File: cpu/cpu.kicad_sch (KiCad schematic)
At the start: 44 parts, among them J2 Conn_01x08, Q1 AO3401A, Q2 RU1J002YN, Q3 RU1J002YN, U1 ICE40HX1K-VQ100_RV4028, U2 W25Q80DVSS, U3 AP2112K-1.2

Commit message: Improve power.  Start work on IO module
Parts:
- removed Q1: AO3401A, Package_TO_SOT_SMD:SOT-23, symbol Transistor_FET:AO3401A
- removed Q2: RU1J002YN, Package_TO_SOT_SMD:SOT-323_SC-70, symbol Transistor_FET:2N7002
- removed R8: 39k, Resistor_SMD:R_0603_1608Metric, symbol Device:R
- removed R9: 3k3, Resistor_SMD:R_0603_1608Metric, symbol Device:R
- removed TP2: Test, TestPoint:TestPoint_Pad_1.5x1.5mm, symbol Connector:TestPoint
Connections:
- net VCCIO is gone; now on net +3V3: C11.2, C12.2, C13.2, C14.2, C15.2, C16.2, C17.2, C18.2, C19.2, C5.1, D1.2 (A), R10.1, R11.1, R3.1, R4.1, R5.1, R6.1, U1.14 (VCCIO_3), U1.22 (VCCIO_3), U1.31 (VCCIO_2), U1.38 (VCCIO_2), U1.50 (VCC_SPI), U1.58 (VCCIO_1), U1.6 (VCCIO_3), U1.67 (VCCIO_1), U1.72 (NC), U1.88 (VCCIO_0), U1.92 (VCCIO_0)
- net +3V3: no longer C3.1, U3.1 (VIN), U3.3 (EN)
- net +5V: now reaches J1.78 (+5V)
- net +5V: now also C3.1, U3.1 (VIN), U3.3 (EN)
- no-connect marks 10 -> 9
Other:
- moved on the sheet: C3, C4, C6, U3

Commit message: RAM module, many tweaks
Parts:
- Q3: value RU1J002YN -> 2N7002; footprint Package_TO_SOT_SMD:SOT-323_SC-70 -> Package_TO_SOT_SMD:SOT-23; JLC C2842817 -> C8545
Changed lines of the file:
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@@
 			)
 		)
-		(property "Value" "RU1J002YN"
+		(property "Value" "2N7002"
 			(at 255.27 120.6499 0)
 			(effects
@@
 			)
 		)
-		(property "Footprint" "Package_TO_SOT_SMD:SOT-323_SC-70"
+		(property "Footprint" "Package_TO_SOT_SMD:SOT-23"
 			(at 254 121.285 0)
 			(effects
@@
 			)
 		)
-		(property "JLC" "C2842817"
+		(property "JLC" "C8545"
 			(at 248.92 119.38 0)
 			(effects

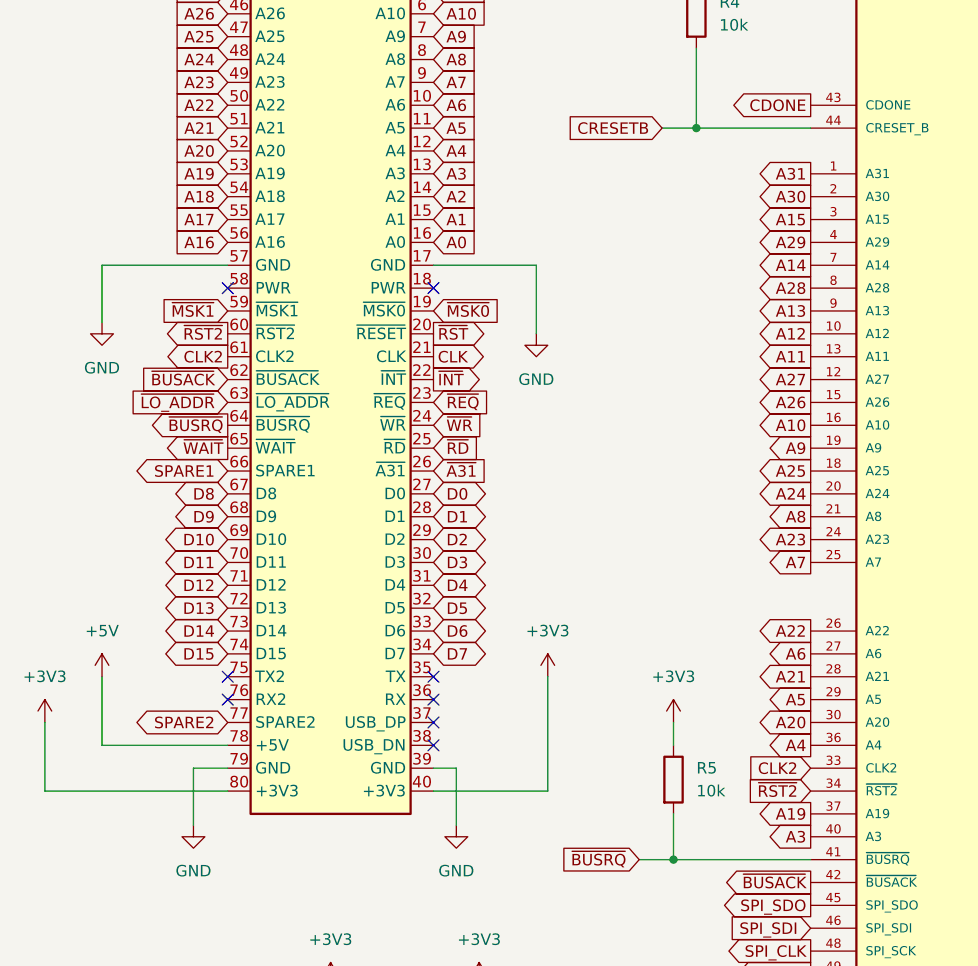
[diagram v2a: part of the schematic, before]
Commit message: Revised module header
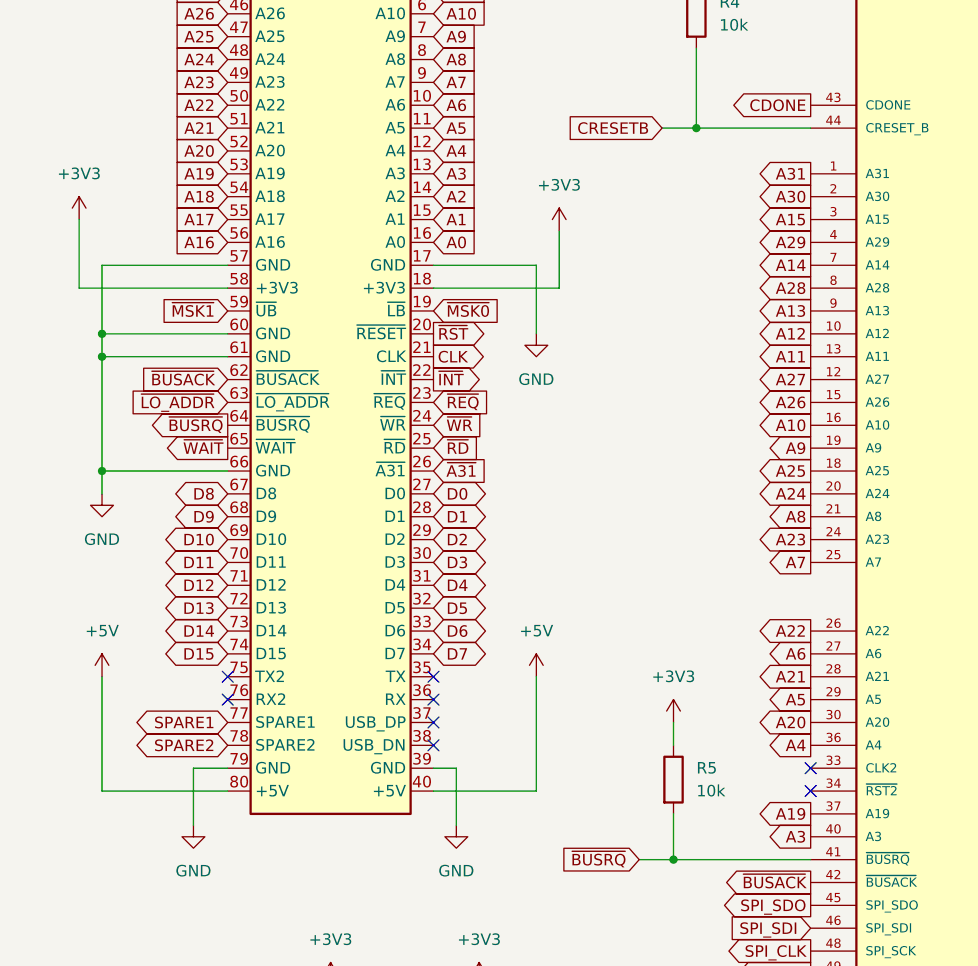
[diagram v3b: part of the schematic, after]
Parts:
- J1: footprint RV4028:ModuleHeader -> RV4028:Module_2mm
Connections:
- net +3V3: now also J1.18 (+3V3), J1.58 (+3V3); no longer J1.40 (+3V3), J1.80 (+3V3)
- net +5V: now also J1.40 (+5V), J1.80 (+5V); no longer J1.78 (+5V)
- net GND: now also J1.60 (GND), J1.61 (GND), J1.66 (GND)
- net SPARE1: now also J1.77 (SPARE1); no longer J1.66 (SPARE1)
- net SPARE2: now also J1.78 (SPARE2); no longer J1.77 (SPARE2)
- net CLK2: no longer names the net of U1.33 (CLK2)
- net CLK2: no longer J1.61 (CLK2)
- net ~{RST2}: no longer names the net of U1.34 (~{RST2})
- net ~{RST2}: no longer J1.60 (~{RST2})

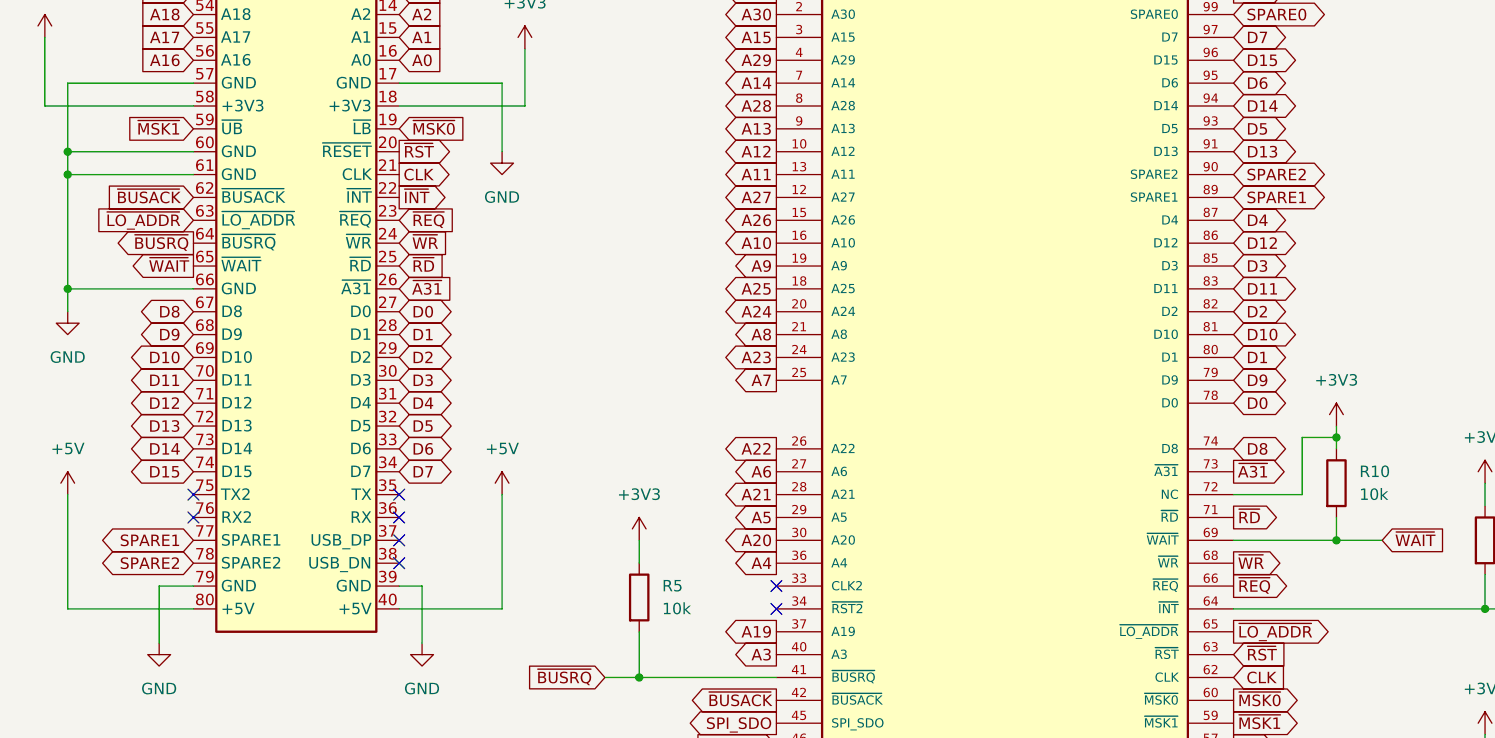
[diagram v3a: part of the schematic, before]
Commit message: IO module 2mm headers
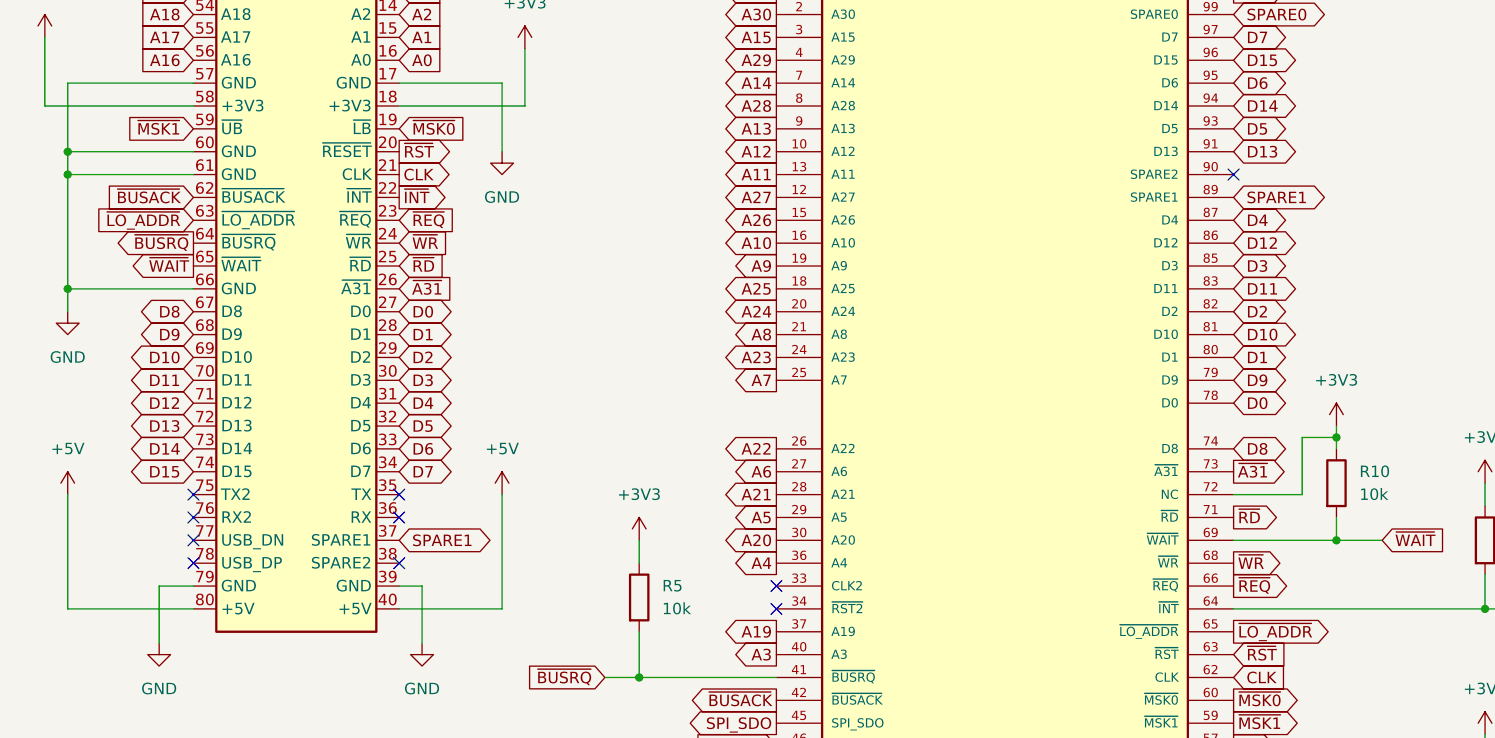
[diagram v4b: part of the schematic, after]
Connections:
- net SPARE1: now also J1.37 (SPARE1); no longer J1.77 (SPARE1)
- net SPARE2: no longer names the net of J1.78 (USB_DP)
- net SPARE2: no longer U1.90 (SPARE2)
- no-connect marks 9 -> 11
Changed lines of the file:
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@@
 	)
 	(no_connect
+		(at 152.4 78.74)
+	)
+	(no_connect
 		(at 152.4 40.64)
 	)
 	(no_connect
+		(at 36.83 121.92)
+	)
+	(no_connect
 		(at 36.83 114.3)
 	)
 	(no_connect
-		(at 59.69 119.38)
+		(at 36.83 119.38)
 	)
 	(wire
@@
 		)
 	)
+	(global_label "SPARE1"
+		(shape bidirectional)
+		(at 59.69 119.38 0)
+		(fields_autoplaced yes)
+		(effects
+			(font
+				(size 1.27 1.27)
+			)
+			(justify left)
+		)
+		(property "Intersheetrefs" "${INTERSHEET_REFS}"
+			(at 70.9831 119.38 0)
+			(effects
+				(font
+					(size 1.27 1.27)
+				)
+				(justify left)
+				(hide yes)
+			)
+		)
+	)
 	(global_label "D10"
 		(shape bidirectional)
@@
 		)
 	)
-	(global_label "SPARE1"
-		(shape bidirectional)
-		(at 36.83 119.38 180)
-		(fields_autoplaced yes)
-		(effects
-			(font
-				(size 1.27 1.27)
-			)
-			(justify right)
-		)
-		(property "Intersheetrefs" "${INTERSHEET_REFS}"
-			(at 25.5369 119.38 0)
-			(effects
-				(font
-					(size 1.27 1.27)
-				)
-				(justify right)
-				(hide yes)
-			)
-		)
-	)
 	(global_label "A17"
 		(shape output)
@@
 		)
 	)
-	(global_label "SPARE2"
-		(shape bidirectional)
-		(at 36.83 121.92 180)
-		(fields_autoplaced yes)
-		(effects
-			(font
-				(size 1.27 1.27)
-			)
-			(justify right)
-		)
-		(property "Intersheetrefs" "${INTERSHEET_REFS}"
-			(at 25.5369 121.92 0)
-			(effects
-				(font
-					(size 1.27 1.27)
-				)
-				(justify right)
-				(hide yes)
-			)
-		)
-	)
 	(global_label "CRESETB"
 		(shape output)
@@
 				(hide yes)
 			)
-		)
-	)
-	(global_label "SPARE2"
-		(shape bidirectional)
-		(at 152.4 78.74 0)
-		(fields_autoplaced yes)
-		(effects
-			(font
-				(size 1.27 1.27)
-			)
-			(justify left)
-		)
-		(property "Intersheetrefs" "${INTERSHEET_REFS}"
-			(at 163.6931 78.74 0)
-			(effects
-				(font
-					(size 1.27 1.27)
-				)
-				(justify left)
-				(hide yes)
-			)

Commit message: CPU and IO production fixes
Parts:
- J1: JLC C3410 -> C3407
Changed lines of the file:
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@@
 			)
 		)
-		(property "JLC" "C3410"
+		(property "JLC" "C3407"
 			(at 48.26 125.73 0)
 			(effects

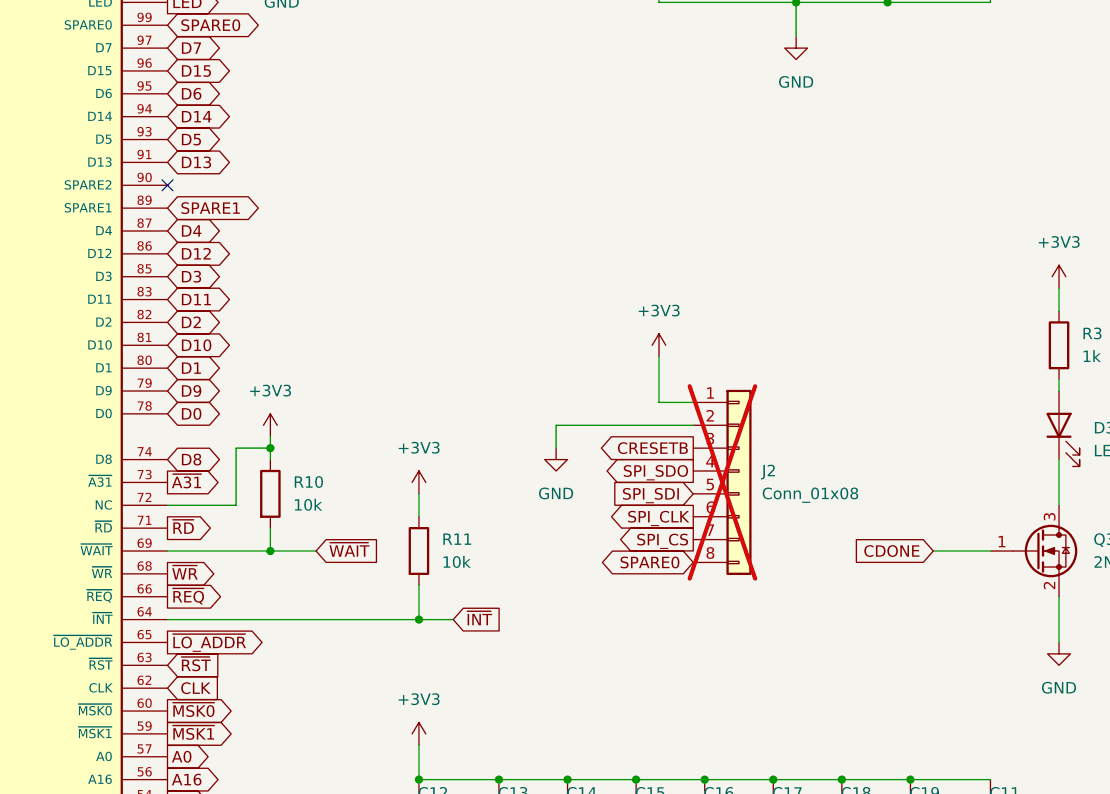
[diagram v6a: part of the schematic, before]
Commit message: Pull up on REQ
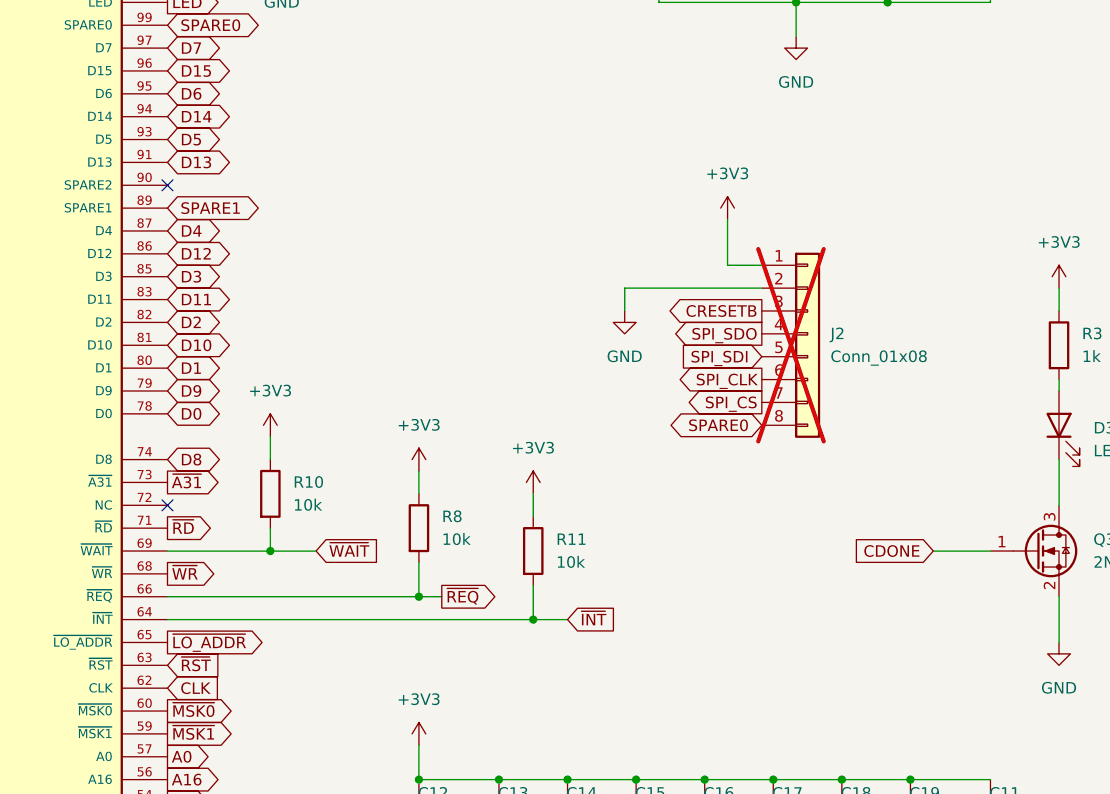
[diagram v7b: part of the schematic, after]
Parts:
- added R8: 10k, Resistor_SMD:R_0402_1005Metric, symbol Device:R
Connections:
- net +3V3: now also R8.1; no longer U1.72 (NC)
- net ~{REQ}: now also R8.2
- no-connect marks 11 -> 12
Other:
- moved on the sheet: J2, R11

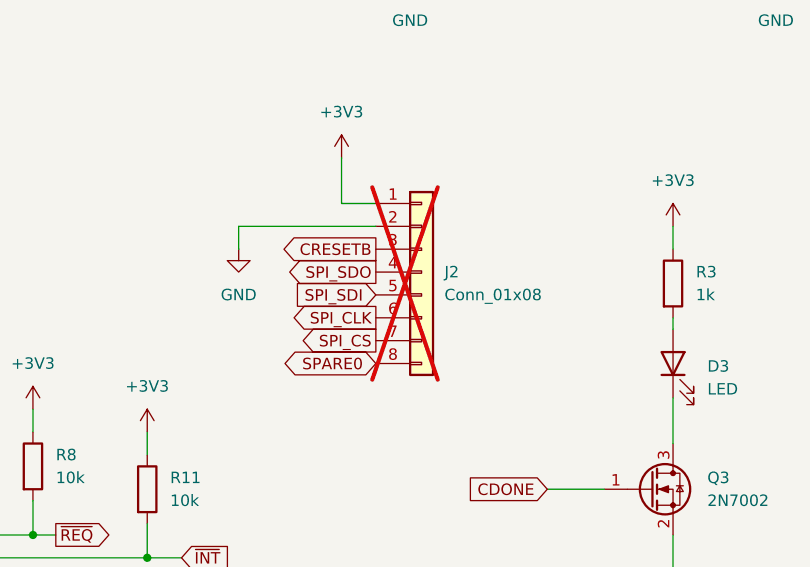
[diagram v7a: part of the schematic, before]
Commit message: Review before first PCB order
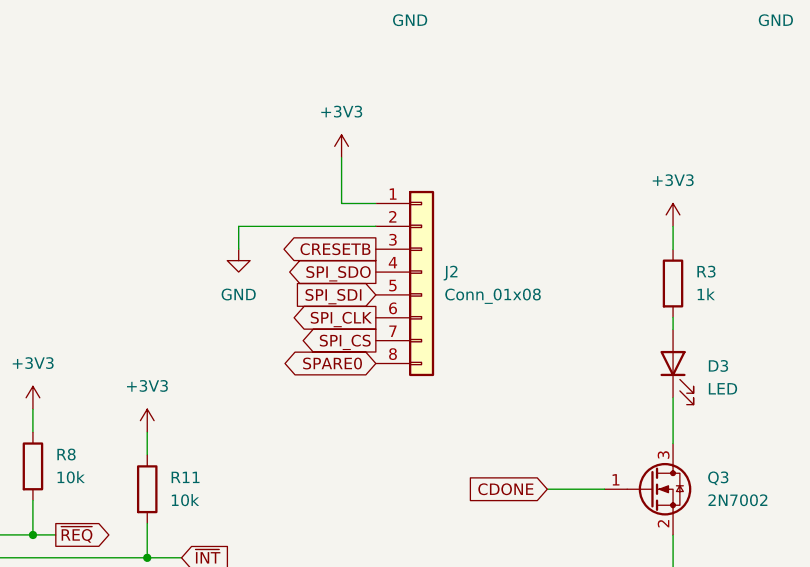
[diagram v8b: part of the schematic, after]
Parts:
- J2: JLC (none) -> C5383116; now fitted
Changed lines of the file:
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@@
 		(in_bom yes)
 		(on_board yes)
-		(dnp yes)
+		(dnp no)
 		(fields_autoplaced yes)
 		(property "Reference" "J2"
@@
 			(at 223.52 95.25 0)
 			(effects
+				(font
+					(size 1.27 1.27)
+				)
+				(hide yes)
+			)
+		)
+		(property "JLC" "C5383116"
+			(at 223.52 95.25 0)
+			(effects
